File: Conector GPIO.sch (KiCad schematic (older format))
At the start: 5 parts, among them P12 CONN_10X2, P14 SPI

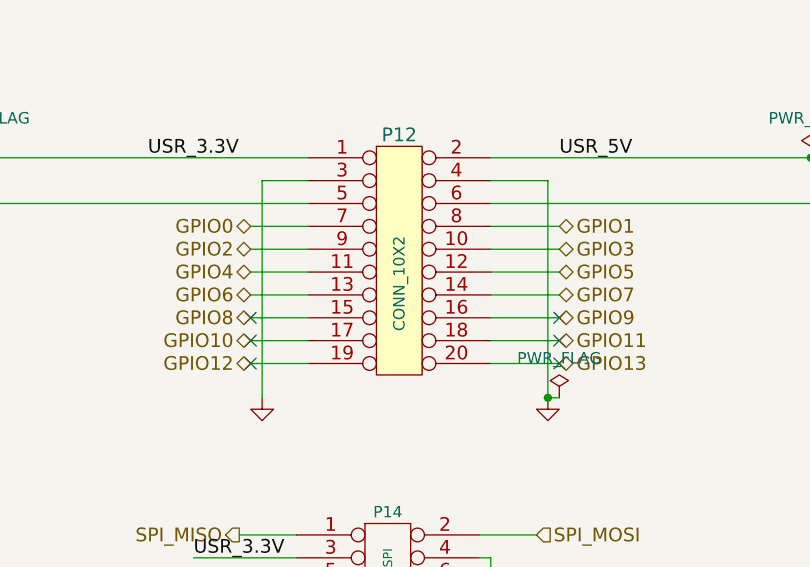
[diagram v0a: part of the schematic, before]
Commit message: eliminado gpio para motores ya que la CIAA no cuenta con suficientes GPIOs disponibles. Se usara DOUTS
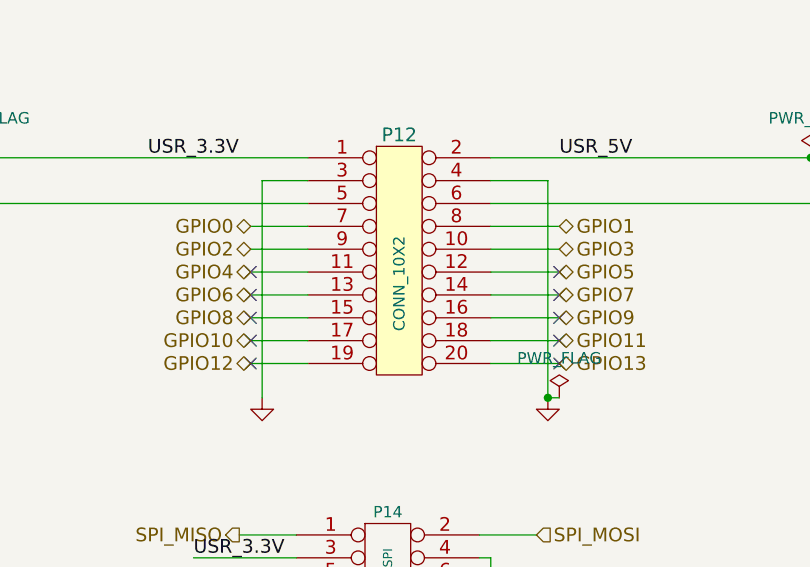
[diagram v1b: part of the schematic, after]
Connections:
- no-connect marks 7 -> 11
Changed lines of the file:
@@
 $Descr A4 11693 8268
 encoding utf-8
-Sheet 2 5
+Sheet 2 4
 Title ""
 Date ""
@@
 	1    0    0    -1
 $EndComp
+NoConn ~ 6600 2350
+NoConn ~ 6600 2250
+NoConn ~ 5250 2250
+NoConn ~ 5250 2350
 $EndSCHEMATC

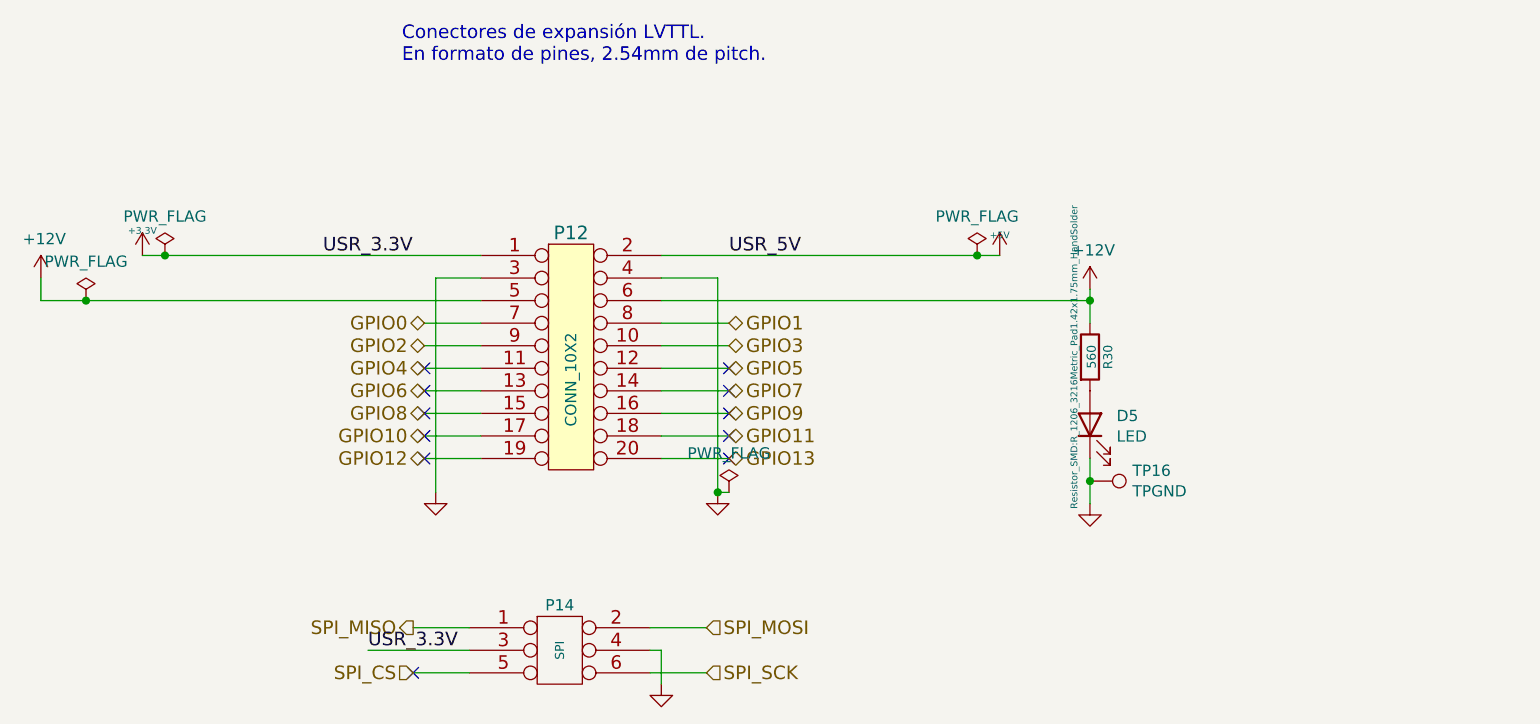
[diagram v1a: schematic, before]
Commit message: Se arregló conexion erronea en los amplificadores operacionales
se agregó conexión 1-wire en GPIO8
se agregó botón y led que comparten GPIO7, la idea es leer el estado del
botón y al liberarlo cambiar el GPIO a output y encender el led indicando
alguna acción
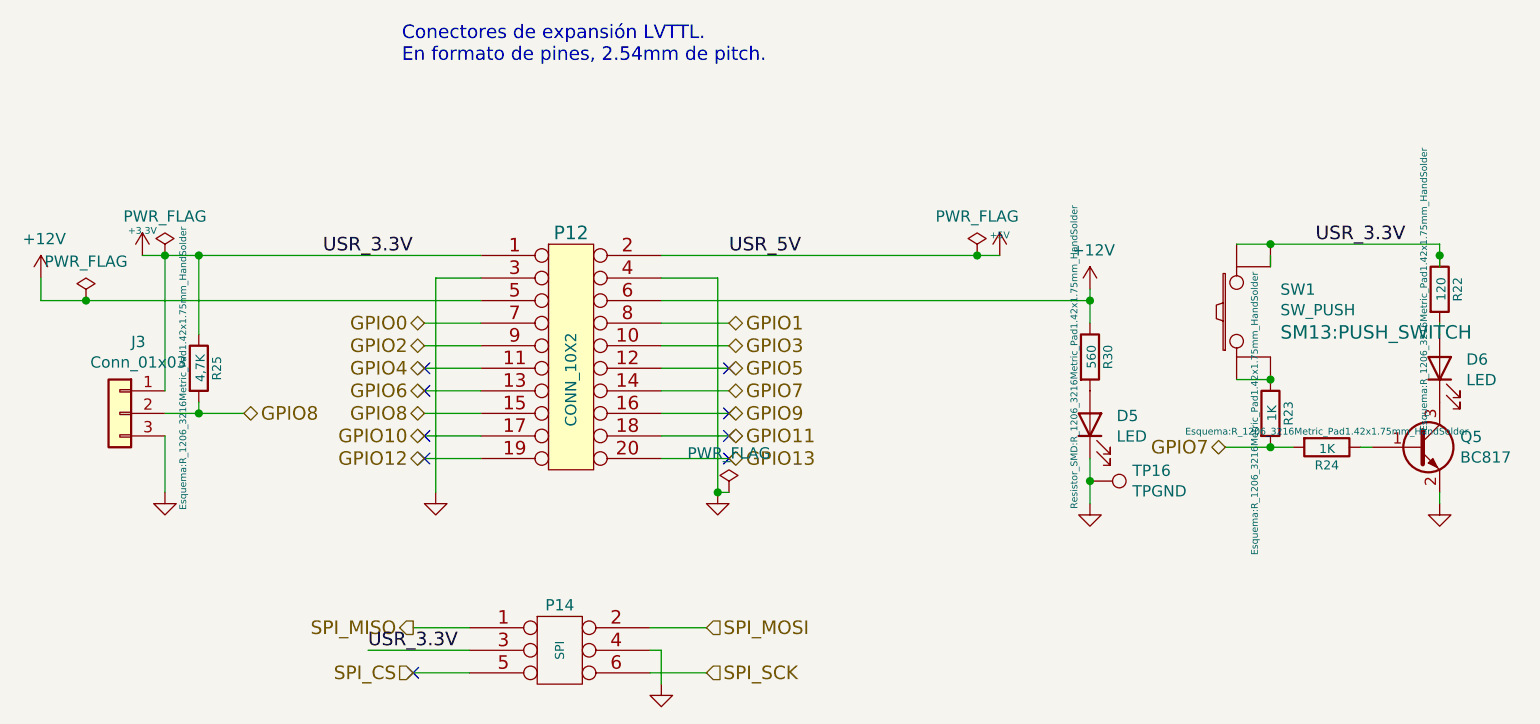
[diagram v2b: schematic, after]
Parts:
- added D6: LED, LED_SMD:LED_1206_3216Metric_Pad1.42x1.75mm_HandSolder, symbol Device:LED
- added J3: Conn_01x03, Connector_Molex:Molex_KK-254_AE-6410-03A_1x03_P2.54mm_Vertical, symbol Connector_Generic:Conn_01x03
- added Q5: BC817, Package_TO_SOT_SMD:SOT-23, symbol Transistor_BJT:BC817
- added R22: 120, Esquema:R_1206_3216Metric_Pad1.42x1.75mm_HandSolder, symbol Device:R
- added R23, R24: 1K, Esquema:R_1206_3216Metric_Pad1.42x1.75mm_HandSolder, symbol Device:R
- added R25: 4,7K, Esquema:R_1206_3216Metric_Pad1.42x1.75mm_HandSolder, symbol Device:R
- added SW1: SW_PUSH, SM13:PUSH_SWITCH, symbol sw_push:SW_PUSH
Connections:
- wire segments 38 -> 56
- no-connect marks 11 -> 9
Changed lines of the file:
@@
 Wire Wire Line
 	5250 2350 5500 2350
-Text HLabel 5250 2450 0    60   BiDi ~ 0
-GPIO8
-Wire Wire Line
-	5250 2450 5500 2450
 Text HLabel 5250 2550 0    60   BiDi ~ 0
 GPIO10
@@
 NoConn ~ 6600 2550
 NoConn ~ 6600 2650
-NoConn ~ 5250 2450
 NoConn ~ 5250 2550
 NoConn ~ 5250 2650
 NoConn ~ 5200 3600
 Wire Wire Line
-	4100 1750 5500 1750
+	4100 1750 4250 1750
 Wire Wire Line
 	6300 1750 7700 1750
@@
 	1    0    0    -1
 $EndComp
-NoConn ~ 6600 2350
 NoConn ~ 6600 2250
 NoConn ~ 5250 2250
 NoConn ~ 5250 2350
+$Comp
+L Connector_Generic:Conn_01x03 J3
+U 1 1 60A706B3
+P 3900 2450
+F 0 "J3" H 3818 2767 50  0000 C CNN
+F 1 "Conn_01x03" H 3818 2676 50  0000 C CNN
+F 2 "Connector_Molex:Molex_KK-254_AE-6410-03A_1x03_P2.54mm_Vertical" H 3900 2450 50  0001 C CNN
+F 3 "~" H 3900 2450 50  0001 C CNN
+	1    3900 2450
+	-1   0    0    -1
+$EndComp
+Text HLabel 5250 2450 0    60   BiDi ~ 0
+GPIO8
+Wire Wire Line
+	5250 2450 5500 2450
+Text HLabel 4450 2450 2    60   BiDi ~ 0
+GPIO8
+$Comp
+L Device:R R?
+U 1 1 60A7541F
+P 4250 2250
+AR Path="/60A7541F" Ref="R?"  Part="1"
+AR Path="/5EF45E27/60A7541F" Ref="R?"  Part="1"
+AR Path="/5F077C82/60A7541F" Ref="R?"  Part="1"
+AR Path="/5EF34214/60A7541F" Ref="R?"  Part="1"
+AR Path="/5EF2A268/60A7541F" Ref="R25"  Part="1"
+F 0 "R25" V 4330 2250 40  0000 C CNN
+F 1 "4,7K" V 4257 2251 40  0000 C CNN
+F 2 "Esquema:R_1206_3216Metric_Pad1.42x1.75mm_HandSolder" V 4180 2250 30  0000 C CNN
+F 3 "~" H 4250 2250 30  0000 C CNN
+	1    4250 2250
+	1    0    0    -1
+$EndComp
+Wire Wire Line
+	4100 2450 4250 2450
+Connection ~ 4250 1750
+Wire Wire Line
+	4250 1750 5500 1750
+Wire Wire Line
+	4250 2400 4250 2450
+Connection ~ 4250 2450
+Wire Wire Line
+	4250 2450 4450 2450
+$Comp
+L power:GND #PWR0104
+U 1 1 60A788BA
+P 4100 2800
+F 0 "#PWR0104" H 4100 2800 30  0001 C CNN
+F 1 "GND" H 4100 2730 30  0001 C CNN
+F 2 "" H 4100 2800 60  0000 C CNN
+F 3 "" H 4100 2800 60  0000 C CNN
+	1    4100 2800
+	1    0    0    -1
+$EndComp
+Wire Wire Line
+	4100 1750 4100 2350
+Wire Wire Line
+	4250 1750 4250 2100
+Wire Wire Line
+	4100 2550 4100 2800
+$Comp
+L Device:R R?
+U 1 1 60A951D4
+P 9750 1900
+AR Path="/60A951D4" Ref="R?"  Part="1"
+AR Path="/5EF45E27/60A951D4" Ref="R?"  Part="1"
+AR Path="/5F077C82/60A951D4" Ref="R?"  Part="1"
+AR Path="/5EF2A268/60A951D4" Ref="R22"  Part="1"
+F 0 "R22" V 9830 1900 40  0000 C CNN
+F 1 "120" V 9757 1901 40  0000 C CNN
+F 2 "Esquema:R_1206_3216Metric_Pad1.42x1.75mm_HandSolder" V 9680 1900 30  0000 C CNN
+F 3 "~" H 9750 1900 30  0000 C CNN
+	1    9750 1900
+	1    0    0    -1
+$EndComp
+$Comp
+L Device:LED D?
+U 1 1 60A951DA
+P 9750 2250
+AR Path="/60A951DA" Ref="D?"  Part="1"
+AR Path="/5EF45E27/60A951DA" Ref="D?"  Part="1"
+AR Path="/5F077C82/60A951DA" Ref="D?"  Part="1"
+AR Path="/5EF2A268/60A951DA" Ref="D6"  Part="1"
+F 0 "D6" V 9789 2132 50  0000 R CNN
+F 1 "LED" V 9698 2132 50  0000 R CNN
+F 2 "LED_SMD:LED_1206_3216Metric_Pad1.42x1.75mm_HandSolder" H 9750 2250 50  0001 C CNN
+F 3 "~" H 9750 2250 50  0001 C CNN
+	1    9750 2250
+	0    -1   -1   0
+$EndComp
+$Comp
+L Device:R R?
+U 1 1 60A951E0
+P 9250 2600
+AR Path="/60A951E0" Ref="R?"  Part="1"
+AR Path="/5EF45E27/60A951E0" Ref="R?"  Part="1"
+AR Path="/5F077C82/60A951E0" Ref="R?"  Part="1"
+AR Path="/5EF2A268/60A951E0" Ref="R24"  Part="1"
+F 0 "R24" V 9330 2600 40  0000 C CNN
+F 1 "1K" V 9257 2601 40  0000 C CNN
+F 2 "Esquema:R_1206_3216Metric_Pad1.42x1.75mm_HandSolder" V 9180 2600 30  0000 C CNN
+F 3 "~" H 9250 2600 30  0000 C CNN
+	1    9250 2600
+	0    1    1    0
+$EndComp
+$Comp
+L power:GND #PWR?
+U 1 1 60AA066E
+P 9750 2850
+AR Path="/60AA066E" Ref="#PWR?"  Part="1"
+AR Path="/5EF34214/60AA066E" Ref="#PWR?"  Part="1"
+AR Path="/5EF2A268/60AA066E" Ref="#PWR0105"  Part="1"
+F 0 "#PWR0105" H 9750 2850 30  0001 C CNN
+F 1 "GND" H 9750 2780 30  0001 C CNN
+F 2 "" H 9750 2850 60  0000 C CNN
+F 3 "" H 9750 2850 60  0000 C CNN
+	1    9750 2850
+	1    0    0    -1
+$EndComp
+Wire Wire Line
+	9750 2800 9750 2850
+Text Label 9200 1700 0    60   ~ 0
+USR_3.3V
+Text HLabel 8800 2600 0    60   BiDi ~ 0
+GPIO7
+Wire Wire Line
+	9000 1750 9000 1800
+Wire Wire Line
+	9400 2600 9450 2600
+$Comp
+L Transistor_BJT:BC817 Q5
+U 1 1 60AAEAE9
+P 9650 2600
+F 0 "Q5" H 9841 2646 50  0000 L CNN
+F 1 "BC817" H 9841 2555 50  0000 L CNN
+F 2 "Package_TO_SOT_SMD:SOT-23" H 9850 2525 50  0001 L CIN
+F 3 "https://www.onsemi.com/pub/Collateral/BC818-D.pdf" H 9650 2600 50  0001 L CNN
+	1    9650 2600
+	1    0    0    -1
+$EndComp
+Wire Wire Line
+	8800 2600 9000 2600
+$Comp
+L Device:R R?
+U 1 1 60A9ED4E
+P 9000 2450
+AR Path="/60A9ED4E" Ref="R?"  Part="1"
+AR Path="/5EF45E27/60A9ED4E" Ref="R?"  Part="1"
+AR Path="/5F077C82/60A9ED4E" Ref="R?"  Part="1"
+AR Path="/5EF2A268/60A9ED4E" Ref="R23"  Part="1"
+F 0 "R23" V 9080 2450 40  0000 C CNN
+F 1 "1K" V 9007 2451 40  0000 C CNN
+F 2 "Esquema:R_1206_3216Metric_Pad1.42x1.75mm_HandSolder" V 8930 2450 30  0000 C CNN
+F 3 "~" H 9000 2450 30  0000 C CNN
+	1    9000 2450
+	1    0    0    -1
+$EndComp
+Connection ~ 9000 2600
+Wire Wire Line
+	9000 2600 9100 2600
+Wire Wire Line
+	9750 1700 9750 1750
+Wire Wire Line
+	9000 1700 9750 1700
+Wire Wire Line
+	8850 1700 9000 1700
+Connection ~ 9000 1700
+Wire Wire Line
+	8850 2300 9000 2300
+Connection ~ 9000 2300
+$Comp
+L sw_push:SW_PUSH SW?
+U 1 1 60AEAB57
+P 8850 2000
+AR Path="/5EF45E27/60AEAB57" Ref="SW?"  Part="1"
+AR Path="/5EF2A268/60AEAB57" Ref="SW1"  Part="1"
+F 0 "SW1" V 8949 1806 50  0000 R CNN
+F 1 "SW_PUSH" V 8858 1806 50  0000 R CNN
+F 2 "SM13:PUSH_SWITCH" V 8759 1806 60  0000 R CNN
+F 3 "" H 8850 2000 60  0000 C CNN
+	1    8850 2000
+	0    -1   -1   0
+$EndComp
+Connection ~ 9750 1750
+Wire Wire Line
+	9750 1750 9750 1800
+Wire Wire Line
+	9750 2050 9750 2100
 $EndSCHEMATC
